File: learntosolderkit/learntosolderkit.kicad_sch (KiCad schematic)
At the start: 0 parts

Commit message: add 555
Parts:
- added C1: C, symbol Device:C
- added R1, R2: R, symbol Device:R
- added U1: NE555P, Package_DIP:DIP-8_W7.62mm, symbol Timer:NE555P
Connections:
- new net: C1.1, R1.2, U1.2 (TR), U1.6 (THR)
- new net: R1.1, R2.2, U1.7 (DIS)
- new net: R2.1, U1.8 (VCC)

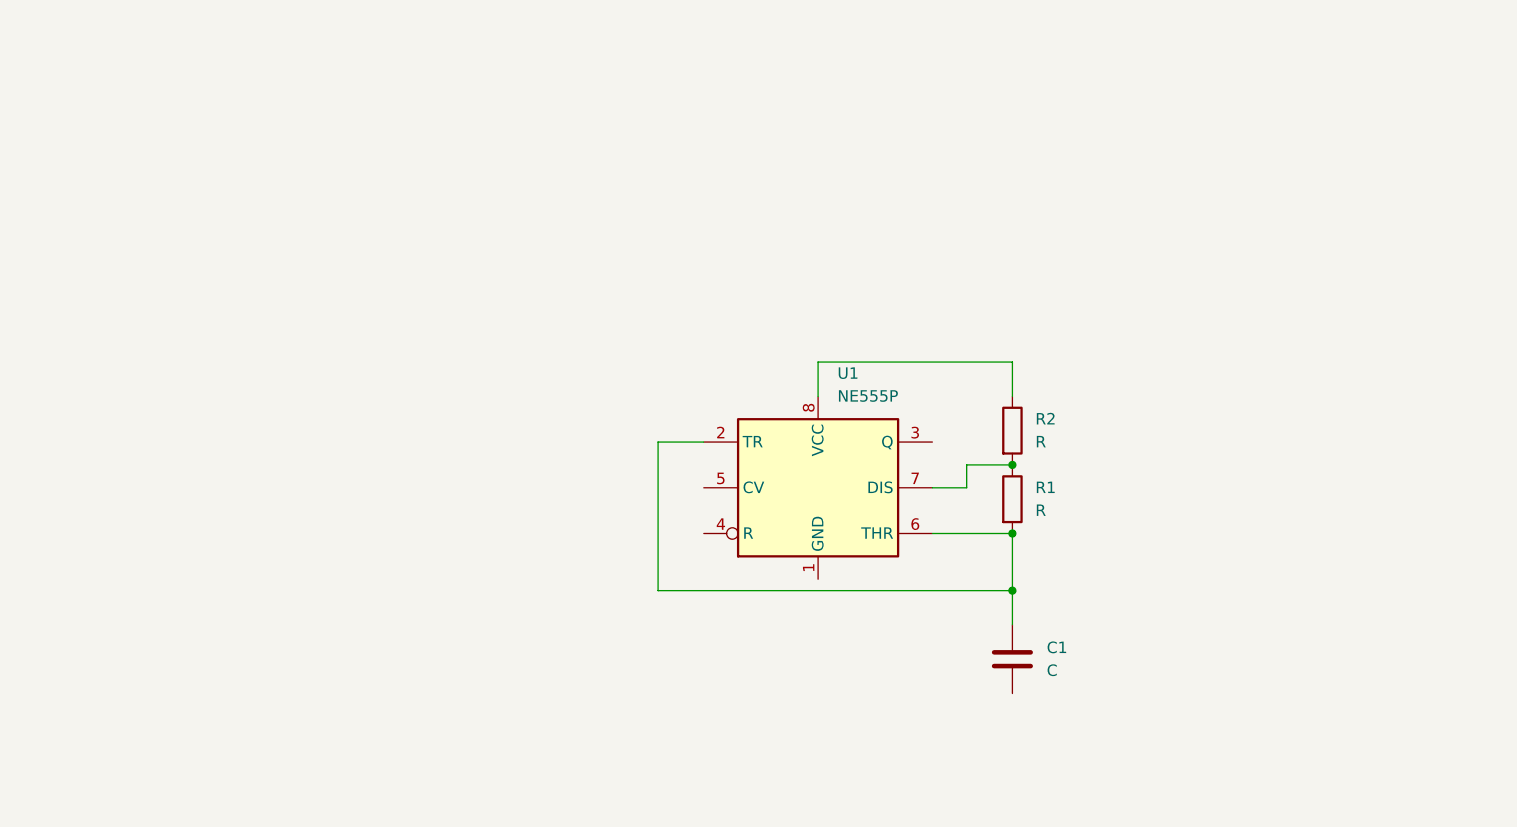
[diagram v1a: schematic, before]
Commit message: place components
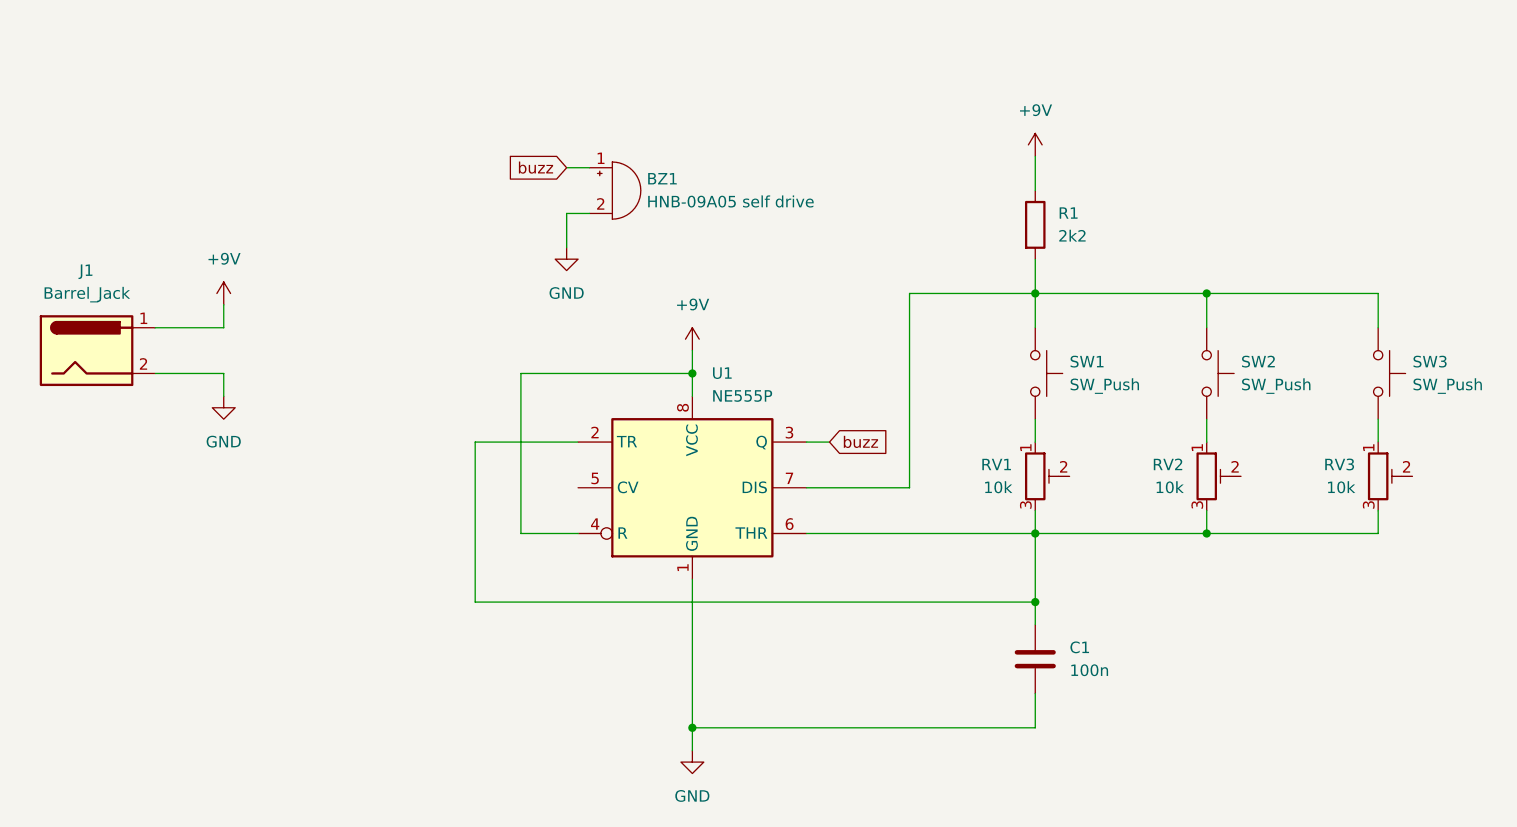
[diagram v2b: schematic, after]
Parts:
- removed R2: R, symbol Device:R
- added BZ1: HNB-09A05 self drive, aaaa_custom:HNB-09A05 buzzer, symbol Device:Buzzer
- added J1: Barrel_Jack, aaaa_custom:9V Battery Connection2THT, symbol Connector:Barrel_Jack
- added RV1, RV2, RV3: 10k, Potentiometer_THT:Potentiometer_Runtron_RM-065_Vertical, symbol Device:R_Potentiometer_Trim
- added SW1, SW2, SW3: SW_Push, Button_Switch_THT:SW_PUSH_6mm, symbol Switch:SW_Push
- C1: value C -> 100n; footprint (none) -> Capacitor_THT:C_Axial_L3.8mm_D2.6mm_P7.50mm_Horizontal
- R1: value R -> 2k2; footprint (none) -> Resistor_THT:R_Axial_DIN0207_L6.3mm_D2.5mm_P10.16mm_Horizontal
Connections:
- net at C1.1, U1.2 (TR), U1.6 (THR): now also RV1.3, RV2.3, RV3.3; no longer R1.2
- net GND: now reaches C1.2
- net GND: now also U1.1 (GND), BZ1.2 (-), J1.2
- net at U1.7 (DIS): now also R1.2, SW1.1, SW2.1, SW3.1; no longer R1.1
- net +9V: now reaches U1.8 (VCC)
- net +9V: now also R1.1, U1.4 (R), J1.1
- net buzz: now reaches U1.3 (Q)
- net buzz: now also BZ1.1 (+)
- new net: RV3.1, SW3.2
- new net: RV1.1, SW1.2
- new net: RV2.1, SW2.2
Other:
- moved on the sheet: C1, U1

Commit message: Finish up
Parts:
- added R2: 330, Resistor_THT:R_Axial_DIN0207_L6.3mm_D2.5mm_P10.16mm_Horizontal, symbol Device:R
- BZ1: value HNB-09A05 self drive -> 42R Passive Buzzer
- C1: value 100n -> 220n
- J1: value Barrel_Jack -> 9V Connector; footprint aaaa_custom:9V Battery Connection2THT -> 1_my_custom_library:9v_dc_batt_2_pin
- RV1, RV2, RV3: footprint Potentiometer_THT:Potentiometer_Runtron_RM-065_Vertical -> 1_my_custom_library:3386P_Trimmer
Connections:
- net buzz: now also R2.1; no longer BZ1.1 (+)
- net at RV3.1: no longer SW3.2
- net at RV3.2: now also C1.1, RV1.2, RV2.2, U1.2 (TR), U1.6 (THR)
- net at RV1.1: no longer SW1.2
- net at SW2.2: now also RV2.3; no longer RV2.1
- new net: RV3.3, SW3.2
- new net: RV1.3, SW1.2
- new net: BZ1.1 (+), R2.2
- no-connect marks 0 -> 3
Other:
- moved on the sheet: R1, RV1, RV2, RV3, SW1, SW2, SW3
